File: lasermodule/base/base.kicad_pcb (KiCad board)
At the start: 2 copper layers, 117 x 60 mm, 64 parts, among them J1 Connector_Generic_Conn_01x02, J2 FPC 15 pin molex vertical, J3 Conn_01x02, J4 Conn_01x03, J5 Conn_01x02, J6 jumper wire 2 pin, U1 DIGIPOT_50K, U10 MCP1700x-330xxTT, U11 LM7808_TO220, U12 ICE40UP5K-SG48ITR-FPGA_Lattice, U13 S25FL064LABMFI010, U14 MCP1700x-120xxTT, U2 U_IC-HKB, U3 STSPIN230, U4 MIC920, U5 MIC920, U6 DRV5033FAxDBZ, U7 DRV5033FAxDBZ, U8 DRV5033FAxDBZ, U9 LM7805_TO220

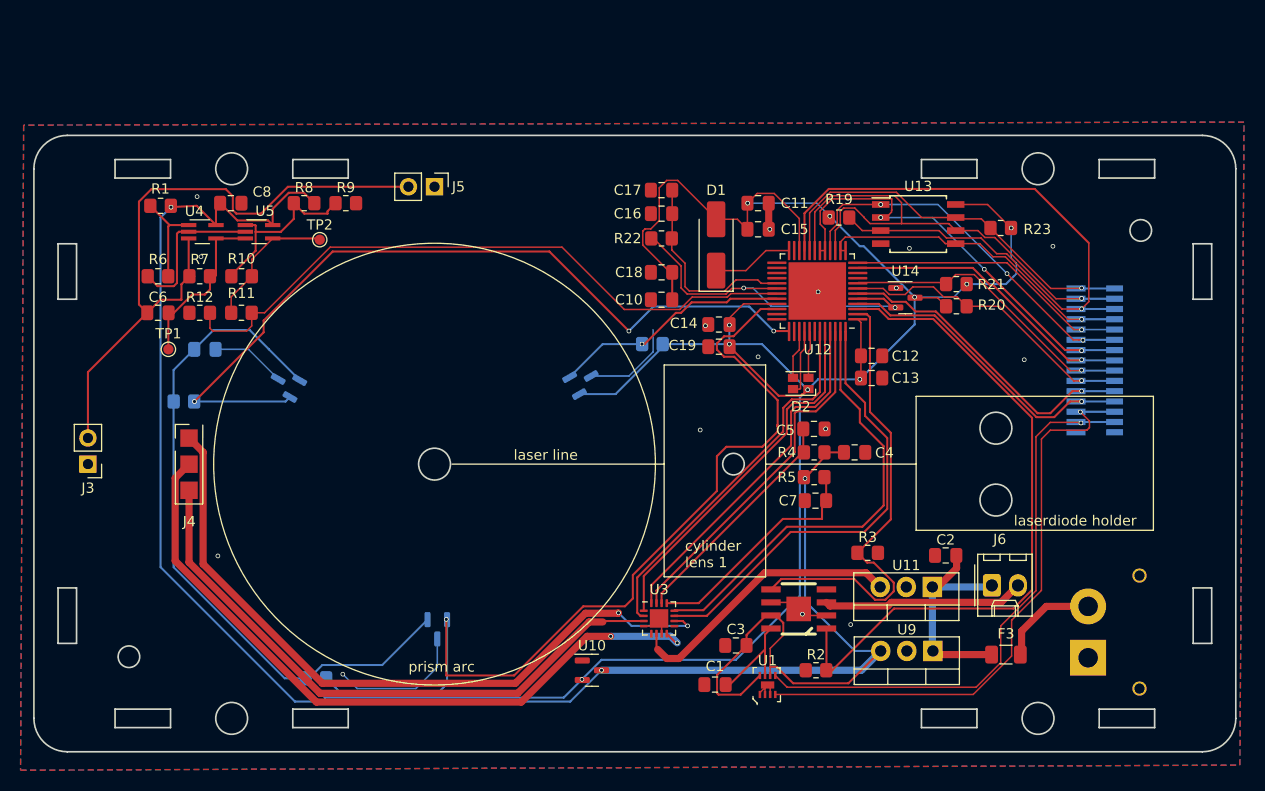
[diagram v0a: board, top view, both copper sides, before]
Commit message: simplified loading in freecad, updated pcbs
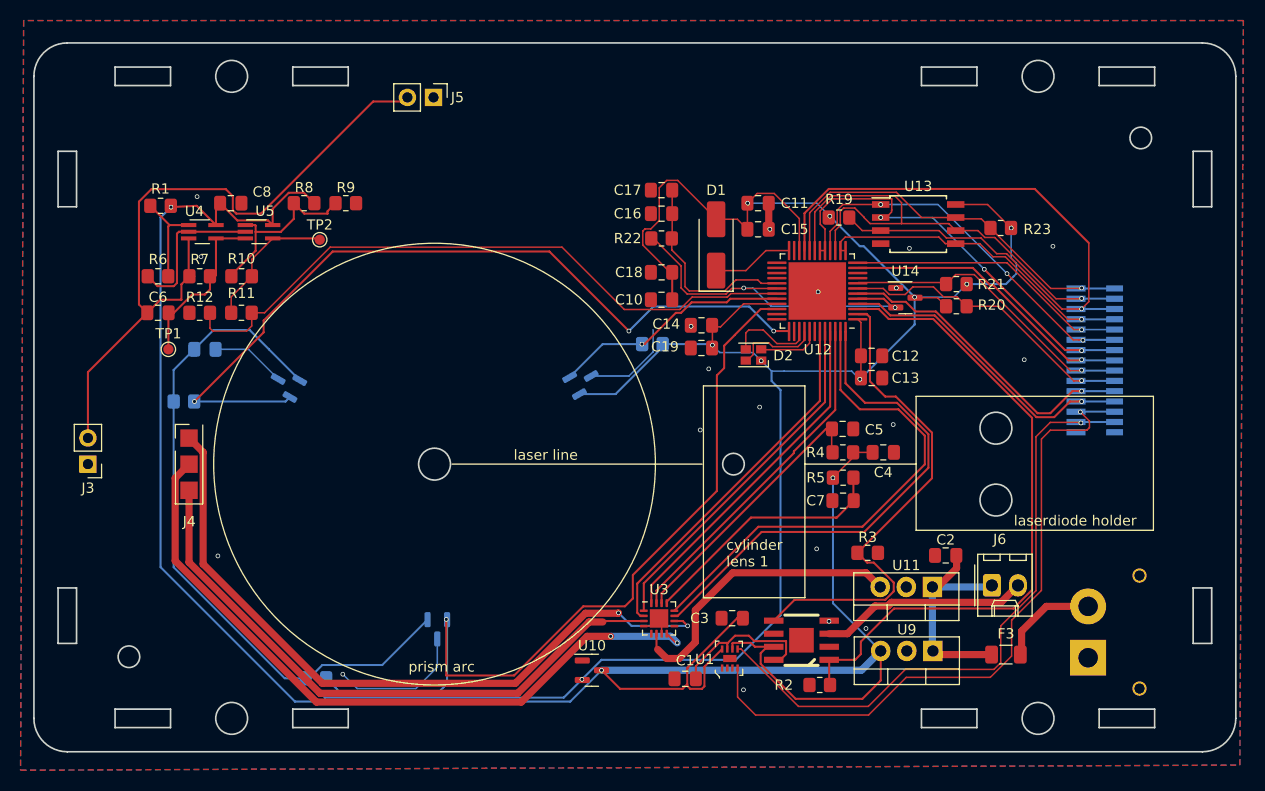
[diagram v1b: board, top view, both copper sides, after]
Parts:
- moved J5 8.70 mm to (104.7, 78.4)
- moved D2 5.37 mm to (135.8, 103.5)
- moved U1 4.48 mm to (133.5, 133.1)
- moved U2 3.06 mm to (140.5, 131.3)
- moved C1 2.96 mm to (129.2, 135.0)
- moved R5 2.82 mm to (144.5, 115.5)
- moved C4 2.79 mm to (148.5, 113.0)
- moved C5 2.79 mm to (144.5, 110.7)
- moved R4 2.79 mm to (144.5, 113.0)
- moved C7 2.68 mm to (144.5, 117.7)
- moved C3 2.68 mm to (133.7, 129.1)
- moved C19 1.71 mm to (130.8, 102.8)
- moved C14 1.70 mm to (130.8, 100.6)
- moved R2 1.48 mm to (142.3, 135.6)
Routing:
- net +5V: track 194.9 -> 206.0 mm
- net GND: track 59.3 -> 50.7 mm, vias 16 -> 19
- net HALL1: track 88.6 -> 80.5 mm
- net POT_SDA: track 57.7 -> 65.7 mm
- net +3V3: track 286.9 -> 279.0 mm, vias 10 -> 9
- net POT_SCL: track 55.6 -> 61.8 mm
- net wH: track 43.3 -> 48.8 mm
- net wL: track 44.0 -> 49.1 mm
- net POT_W: track 10.1 -> 14.8 mm
- net Net-(U3-STBY): track 22.8 -> 26.5 mm
- net RGB0: track 4.77 -> 8.46 mm
- net Net-(J3-Pin_2): track 65.7 -> 69.2 mm
- net IC_HB_PWM1: track 45.6 -> 48.8 mm
- net Net-(U3-EN/FLT): track 22.8 -> 24.7 mm
- net RGB1: track 6.45 -> 8.32 mm
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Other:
- board size 117 x 60 mm -> 117 x 69 mm
